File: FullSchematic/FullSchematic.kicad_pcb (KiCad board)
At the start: 4 copper layers, 155 x 136 mm, 106 parts, among them J1 USB_A, J10 LCD_Conn, J2 ATX-24, J3 Red Banana Jack, J4 Black Banana Jack, J5 2x6 Pin Header, J6 2x6 Pin Header, J7 CT3151-2, J8 CT3151-2, J9 2x6 Pin Header, Q1 BSS138-7-F, Q2 BSS138-7-F, Q3 NPN, SW1 Rotary Switch, U1 IR2181STRPBF, U10 SN74LVC2T45DCURE4, U11 SN74LVC2T45DCURE4, U12 SN74LVC2T45DCURE4, U13 SN74LVC2T45DCURE4, U14 SN74LV595ARGYR, U2 IR2181STRPBF, U3 IPB009N03L G, U4 IPB009N03L G, U5 IPB009N03L G, U6 IPB009N03L G, U7 Current Sensor, U8 Op Amp, U9 L79L05ABD13TR

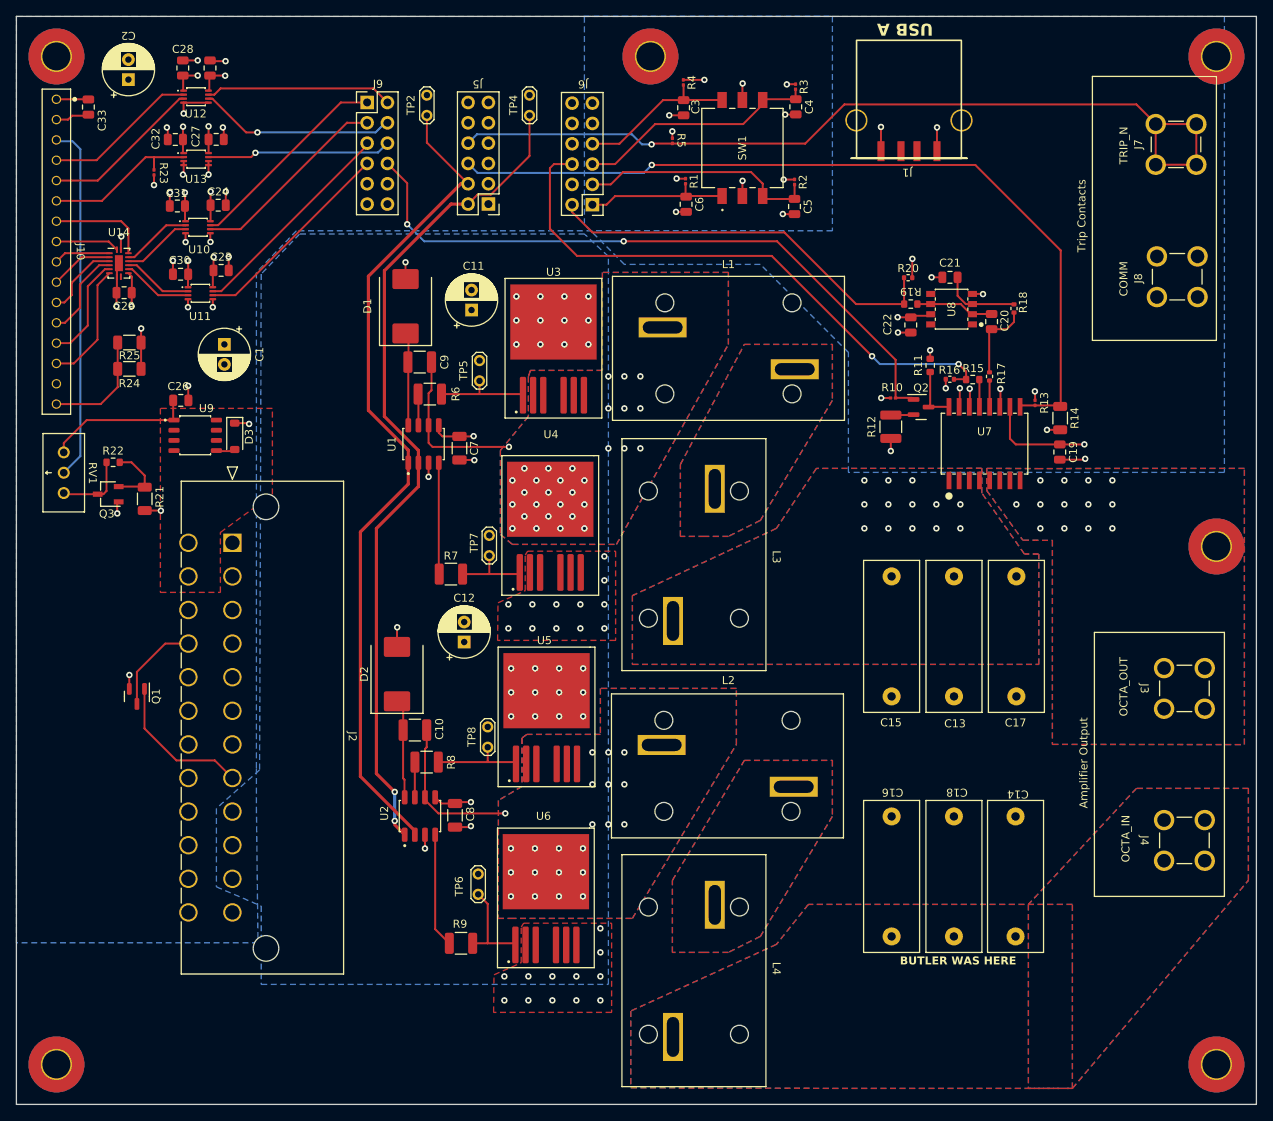
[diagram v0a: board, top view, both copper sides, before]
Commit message: PCB V.4
Fixed power plane issues, cleaned up silk screen, cleaned up via stitching, changed ATX connector to one perpendicular with the board.
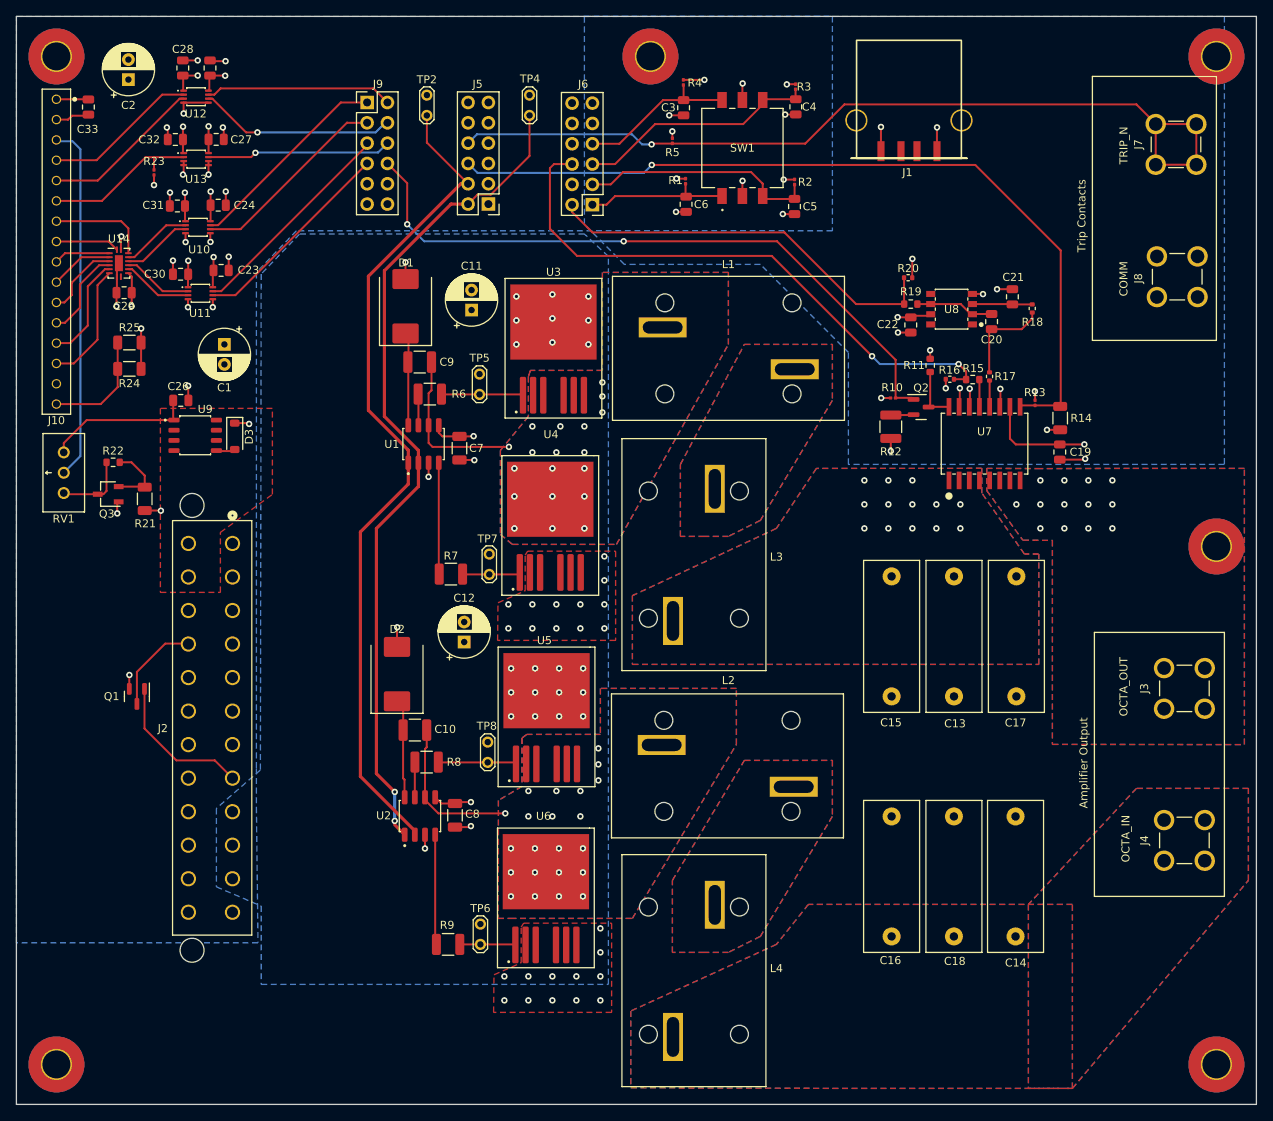
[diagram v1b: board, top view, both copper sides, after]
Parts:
- J2: footprint CustomFootprints:CON_39291247 -> CustomFootprints:CONN_442060001_MOL
- moved C21 8.17 mm to (184.5, 59.0), turned to 90 degrees
- moved TP6 6.26 mm to (118.0, 140.0)
- moved TP7 2.34 mm to (119.1, 93.8)
- moved R18 2.28 mm to (187.0, 60.5)
- moved TP8 1.90 mm to (118.9, 117.2)
- moved TP5 1.69 mm to (117.9, 71.2)
- moved R9 1.62 mm to (114.0, 140.0)
- moved J2 0.08 mm to (87.0, 89.9), turned to -90 degrees
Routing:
- net Net-(U6-Gate): track 12.0 -> 6.98 mm
- net Net-(U8-+IN): track 9.81 -> 7.70 mm
- net Net-(C20-Pad2): track 9.90 -> 11.9 mm
- net Net-(U4-Gate): track 9.24 -> 7.26 mm
- net Net-(U5-Gate): track 11.7 -> 10.1 mm
- net Net-(U3-Gate): track 12.0 -> 10.6 mm
- net Net-(U1-VS): track 42.8 -> 41.8 mm, vias 31 -> 19
- net COM: track 85.4 -> 86.0 mm
- net Net-(U2-LO): track 14.3 -> 13.8 mm
- net +12V: vias 28 -> 25

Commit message: Added silkscreen diodes for real
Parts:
- added D3: MURS320T3G, Diode_SMD:D_SMC, F.Cu at (113.1, 85.2)
- added D4: MURS320T3G, Diode_SMD:D_SMC, F.Cu at (113.6, 132.5)
- moved C11 19.7 mm to (97.2, 59.5)
- moved C12 19.2 mm to (96.8, 101.4)
- moved D1 2.57 mm to (110.9, 61.5), turned to 0 degrees
- moved R6 1.60 mm to (110.2, 70.7)
- moved TP3 1.60 mm to (116.4, 70.7)
- moved U1 1.60 mm to (109.4, 76.9)
- moved C9 1.60 mm to (108.9, 66.7)
- moved C7 1.60 mm to (113.9, 77.5)
- turned TP4 to -90 degrees
- turned TP5 to -90 degrees
- renumbered D3 to D5, TP2 to TP1, TP4 to TP2, TP5 to TP3, TP6 to TP4, TP7 to TP5, TP8 to TP6
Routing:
- net Net-(D3-A): track 41.8 -> 43.8 mm
- net Net-(D1-K): track 11.8 -> 13.3 mm
- net Net-(U3-Gate): track 10.6 -> 12.0 mm
- net Net-(U1-LO): track 13.9 -> 15.1 mm
- net +12V: vias 25 -> 31
- added copper zone on F.Cu, net +12V

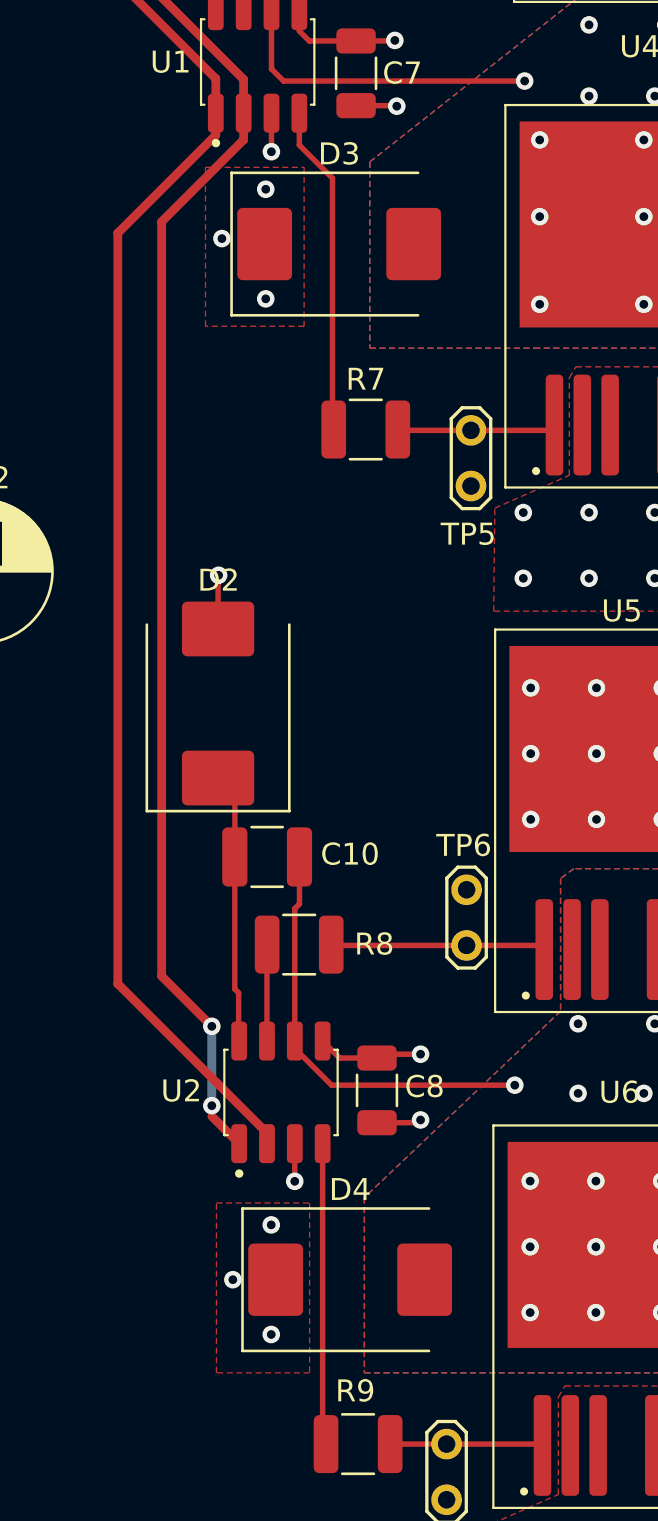
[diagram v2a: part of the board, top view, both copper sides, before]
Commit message: Adjusted placement of flyback diodes
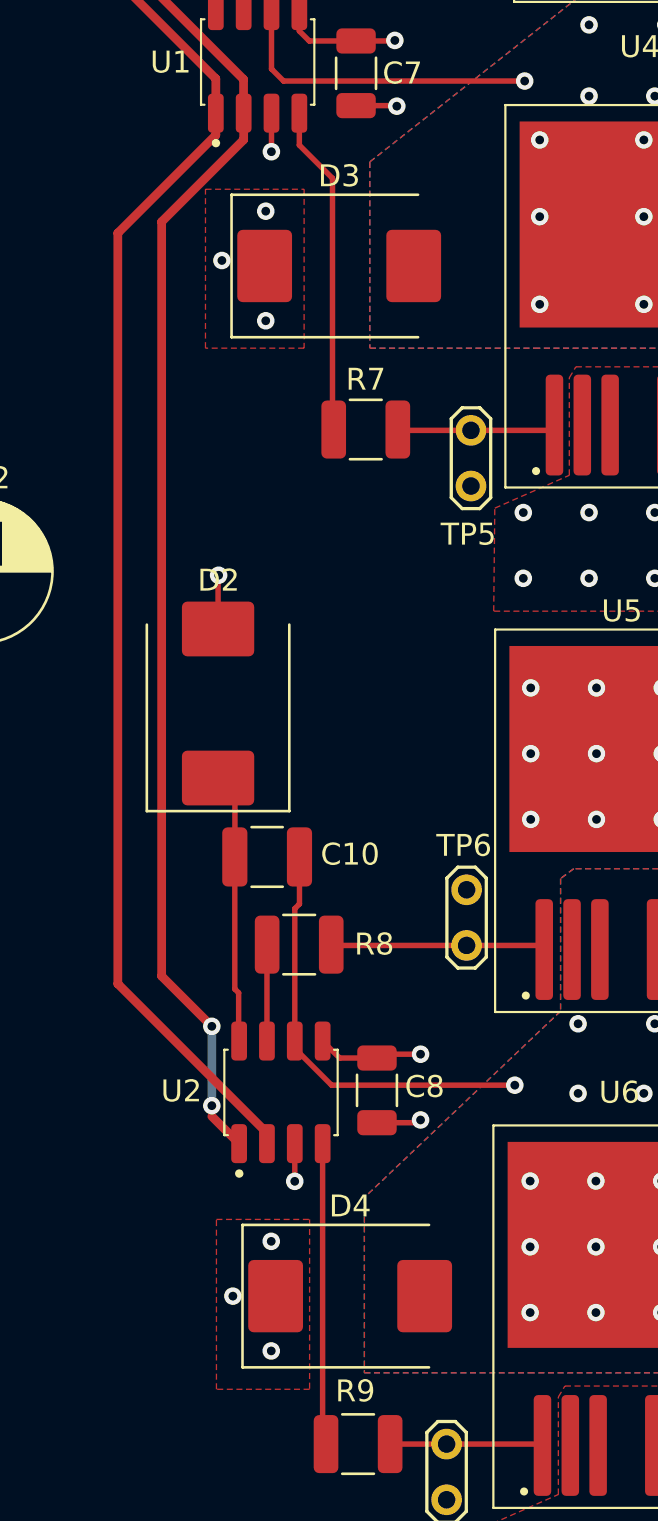
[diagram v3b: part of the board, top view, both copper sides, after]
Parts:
- moved D3 1.00 mm to (113.1, 86.2)
- moved D4 0.75 mm to (113.6, 133.2)
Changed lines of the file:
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@@
   )
   (footprint "Diode_SMD:D_SMC" (layer "F.Cu")
-    (at 113.6 132.5)
+    (at 113.6 133.25)
     (descr "Diode SMC (DO-214AB)")
     (tags "Diode SMC (DO-214AB)")
@@
   )
   (footprint "Diode_SMD:D_SMC" (layer "F.Cu")
-    (at 113.1 85.25)
+    (at 113.1 86.25)
     (descr "Diode SMC (DO-214AB)")
     (tags "Diode SMC (DO-214AB)")
@@
   (segment (start 113.87 75.984) (end 115.615 75.984) (width 0.25) (layer "F.Cu") (net 8))
   (segment (start 111.735 75.984) (end 113.87 75.984) (width 0.25) (layer "F.Cu") (net 8))
-  (via (at 109.75 87.75) (size 0.8) (drill 0.4) (layers "F.Cu" "B.Cu") (free) (net 8))
+  (via (at 109.75 88.75) (size 0.8) (drill 0.4) (layers "F.Cu" "B.Cu") (free) (net 8))
   (via (at 121.84 105.5) (size 0.8) (drill 0.4) (layers "F.Cu" "B.Cu") (net 8))
   (via (at 127.84 111.5) (size 0.8) (drill 0.4) (layers "F.Cu" "B.Cu") (net 8))
-  (via (at 108.25 132.5) (size 0.8) (drill 0.4) (layers "F.Cu" "B.Cu") (free) (net 8))
+  (via (at 108.25 133.25) (size 0.8) (drill 0.4) (layers "F.Cu" "B.Cu") (free) (net 8))
   (via (at 124.84 105.5) (size 0.8) (drill 0.4) (layers "F.Cu" "B.Cu") (net 8))
   (via (at 130.84 111.5) (size 0.8) (drill 0.4) (layers "F.Cu" "B.Cu") (net 8))
@@
   (via (at 121.84 108.5) (size 0.8) (drill 0.4) (layers "F.Cu" "B.Cu") (net 8))
   (via (at 107.6 100.36) (size 0.8) (drill 0.4) (layers "F.Cu" "B.Cu") (net 8))
-  (via (at 110 135) (size 0.8) (drill 0.4) (layers "F.Cu" "B.Cu") (free) (net 8))
+  (via (at 110 135.75) (size 0.8) (drill 0.4) (layers "F.Cu" "B.Cu") (free) (net 8))
   (via (at 122.5 59.007) (size 0.8) (drill 0.4) (layers "F.Cu" "B.Cu") (net 8))
   (via (at 115.64 75.959) (size 0.8) (drill 0.4) (layers "F.Cu" "B.Cu") (net 8))
@@
   (via (at 116.813 122.212) (size 0.8) (drill 0.4) (layers "F.Cu" "B.Cu") (net 8))
   (via (at 121.84 111.5) (size 0.8) (drill 0.4) (layers "F.Cu" "B.Cu") (net 8))
-  (via (at 109.75 82.75) (size 0.8) (drill 0.4) (layers "F.Cu" "B.Cu") (free) (net 8))
+  (via (at 109.75 83.75) (size 0.8) (drill 0.4) (layers "F.Cu" "B.Cu") (free) (net 8))
   (via (at 131.5 62) (size 0.8) (drill 0.4) (layers "F.Cu" "B.Cu") (net 8))
-  (via (at 110 130) (size 0.8) (drill 0.4) (layers "F.Cu" "B.Cu") (free) (net 8))
+  (via (at 110 130.75) (size 0.8) (drill 0.4) (layers "F.Cu" "B.Cu") (free) (net 8))
   (via (at 127.84 105.5) (size 0.8) (drill 0.4) (layers "F.Cu" "B.Cu") (net 8))
   (via (at 127 64.75) (size 0.8) (drill 0.4) (layers "F.Cu" "B.Cu") (net 8))
@@
   (via (at 131.5 65) (size 0.8) (drill 0.4) (layers "F.Cu" "B.Cu") (net 8))
   (via (at 122.5 62) (size 0.8) (drill 0.4) (layers "F.Cu" "B.Cu") (net 8))
-  (via (at 107.75 85) (size 0.8) (drill 0.4) (layers "F.Cu" "B.Cu") (free) (net 8))
+  (via (at 107.75 86) (size 0.8) (drill 0.4) (layers "F.Cu" "B.Cu") (free) (net 8))
   (via (at 130.84 108.5) (size 0.8) (drill 0.4) (layers "F.Cu" "B.Cu") (net 8))
   (via (at 127 61.75) (size 0.8) (drill 0.4) (layers "F.Cu" "B.Cu") (net 8))
@@
     (polygon
       (pts
-        (xy 107 81.75)
-        (xy 111.5 81.75)
-        (xy 111.5 89)
-        (xy 107 89)
+        (xy 107 82.75)
+        (xy 111.5 82.75)
+        (xy 111.5 90)
+        (xy 107 90)
       )
     )
@@
     (polygon
       (pts
-        (xy 111.75 129)
-        (xy 111.75 136.75)
-        (xy 107.5 136.75)
-        (xy 107.5 129)
+        (xy 111.75 129.75)
+        (xy 111.75 137.5)
+        (xy 107.5 137.5)
+        (xy 107.5 129.75)
       )
     )
